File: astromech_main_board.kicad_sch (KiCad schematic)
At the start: 87 parts, among them IC1 MAX11645EUA+, J1 Screw_Terminal_01x02, J10 Conn_01x05, J11 Conn_01x06, J12 Conn_01x04, J13 Conn_01x05, J14 Conn_01x04, J15 Conn_01x04, J19 Conn_01x04, J2 Screw_Terminal_01x02, J20 Conn_01x04, J21 Conn_01x04, J3 Screw_Terminal_01x02, J4 IO_XPAND, J5 Conn_01x06, J6 Conn_01x06, J7 Conn_01x08, J8 Conn_01x03, J9 Conn_01x06, U1 TCA9554DW, U10 LS7366R, U11 LS7366R, U2 TCA9554DW, U3 NCP1117-3.3_SOT223, U4 NCP1117-5.0_TO252, U5 SC16IS752IPW_128, U6 TXB0108PW, U7 TCA9517ADGK, U8 74HC14, U9 LS7366R, Y1 Crystal, Y2 Crystal

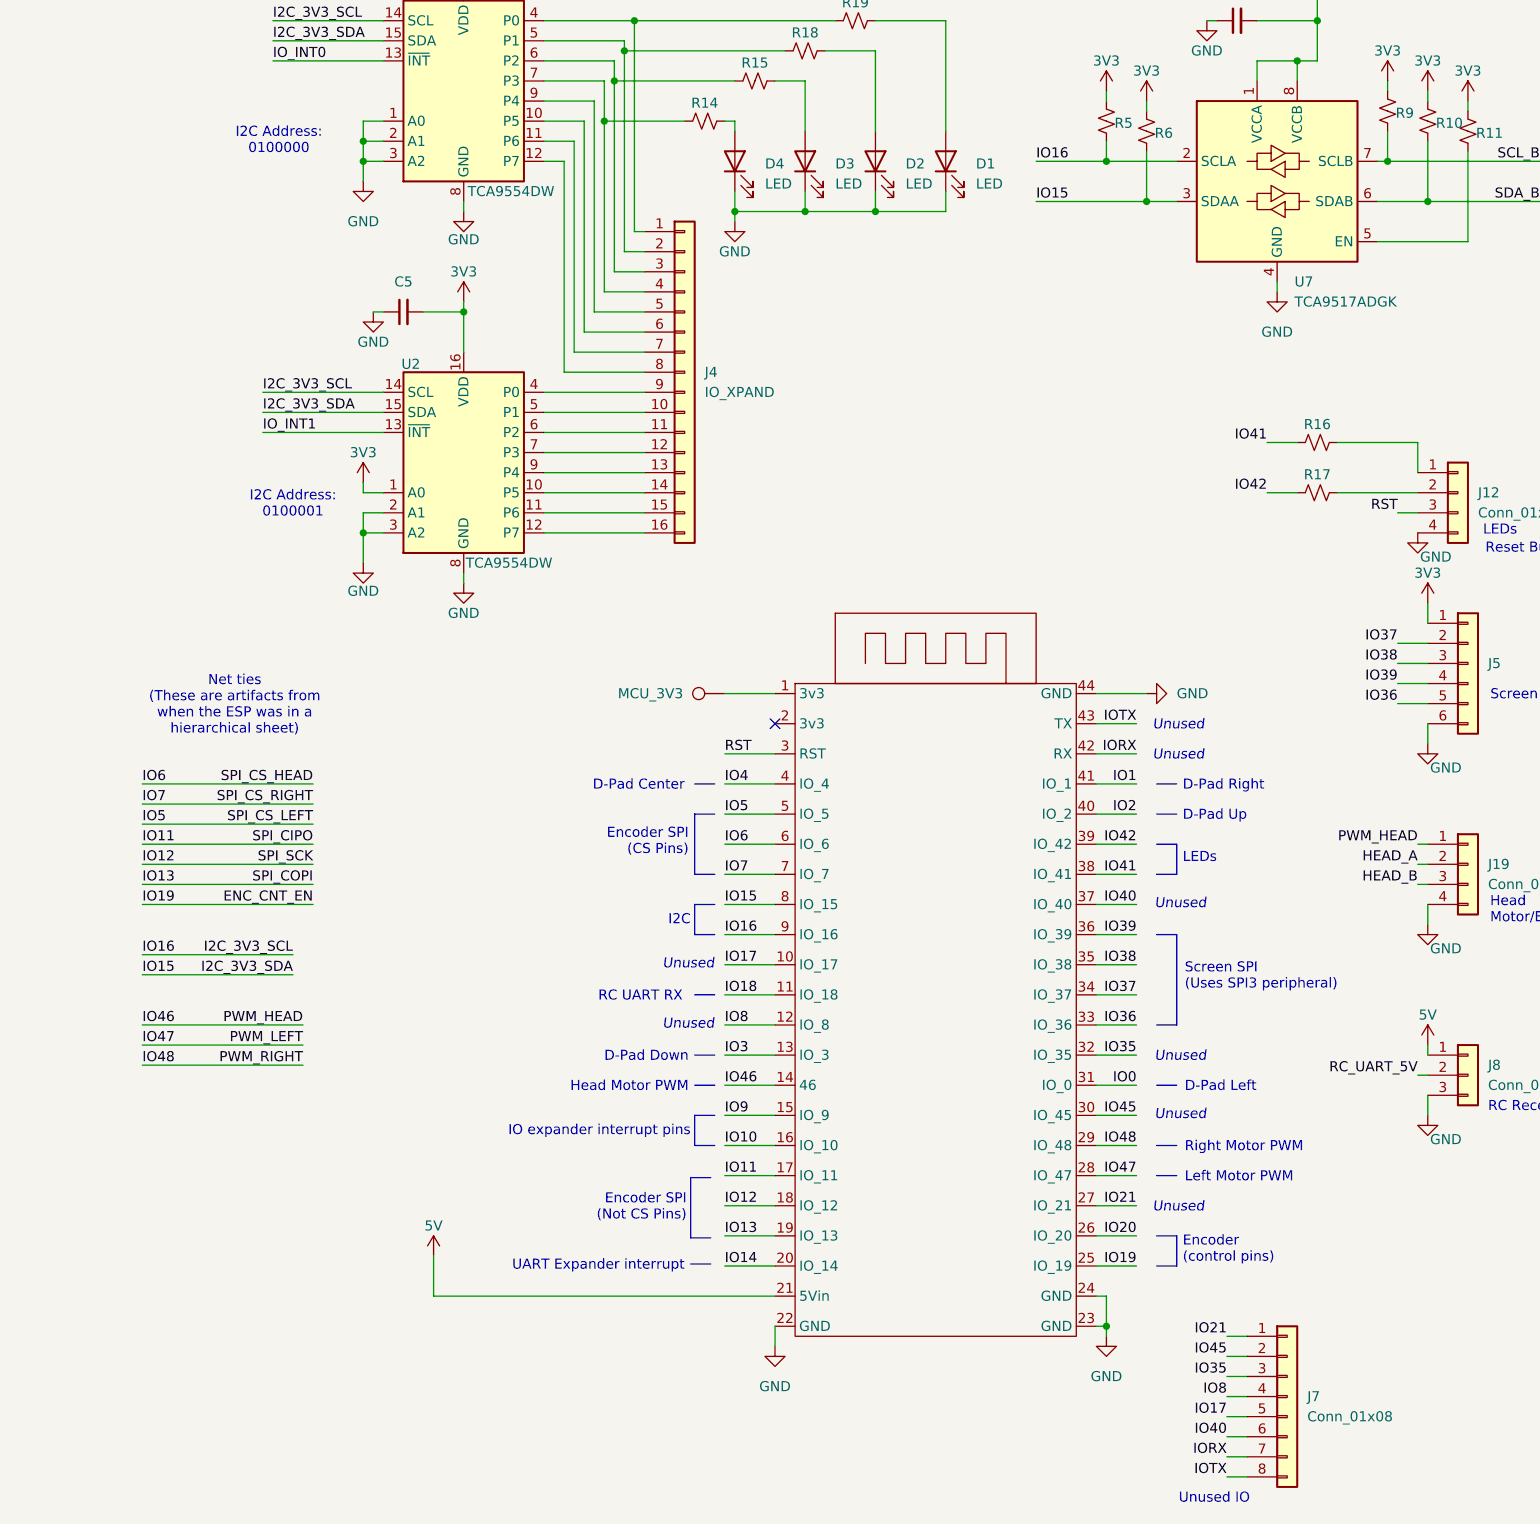
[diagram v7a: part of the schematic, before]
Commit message: renamed nets
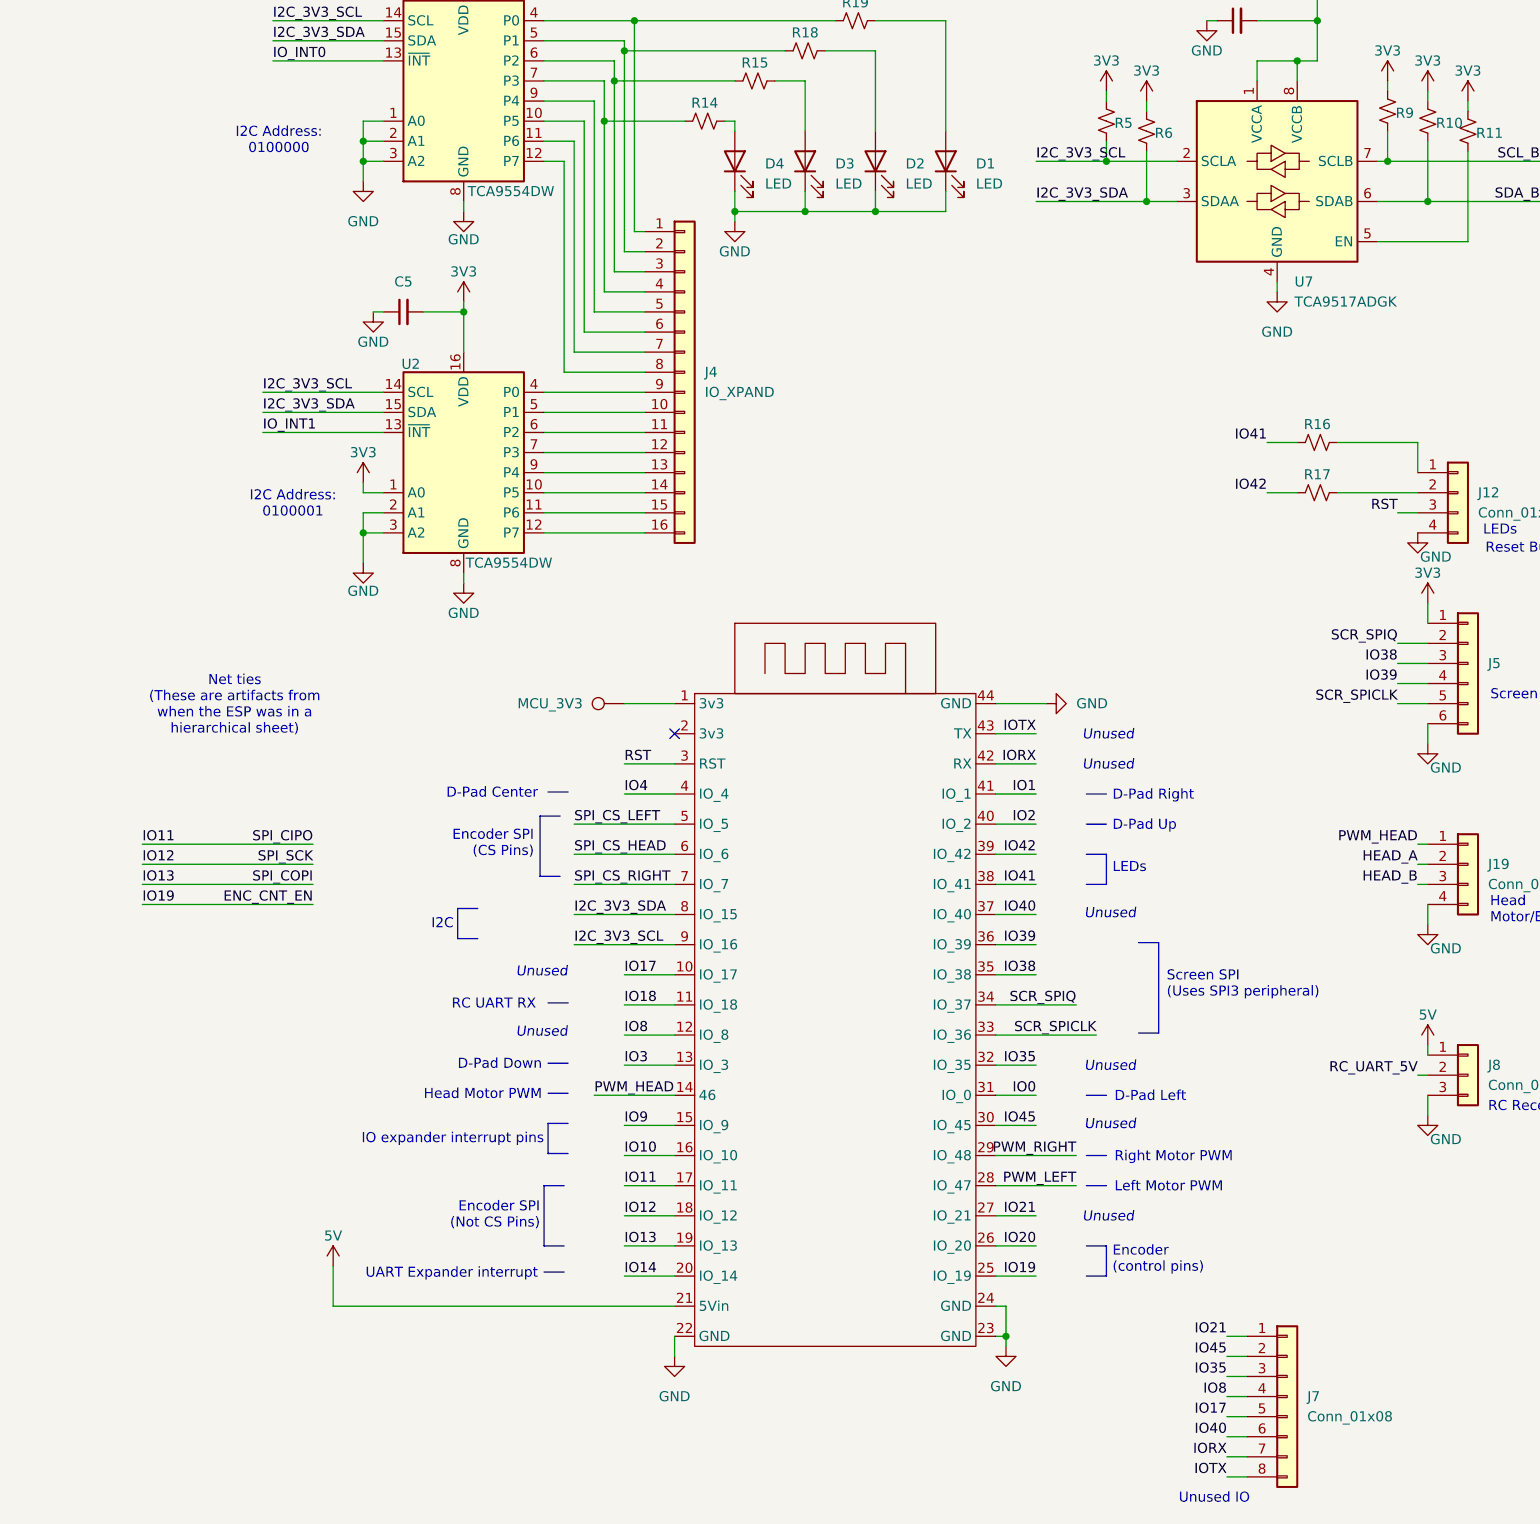
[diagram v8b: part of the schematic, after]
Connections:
- net IO36 renamed SCR_SPICLK
- net IO37 renamed SCR_SPIQ
- net IO46 renamed PWM_HEAD
- net IO47 renamed PWM_LEFT
- net IO48 renamed PWM_RIGHT
- net IO5 renamed SPI_CS_LEFT
- net IO6 renamed SPI_CS_HEAD
- net IO7 renamed SPI_CS_RIGHT
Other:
- moved on the sheet: MCU_3V3
